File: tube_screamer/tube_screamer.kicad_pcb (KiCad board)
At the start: 2 copper layers, 80 x 100 mm, 68 parts, among them J1 Jack_6.35, J2 Jack_6.35, J3 Conn_01x05, J4 Conn_01x05, J5 Conn_01x05, J6 Barrel_Jack_Switch, J7 Conn_01x01_Socket, J8 Conn_01x01_Socket, P1 tube_screamer_front_panel, Q1 MMBT5551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

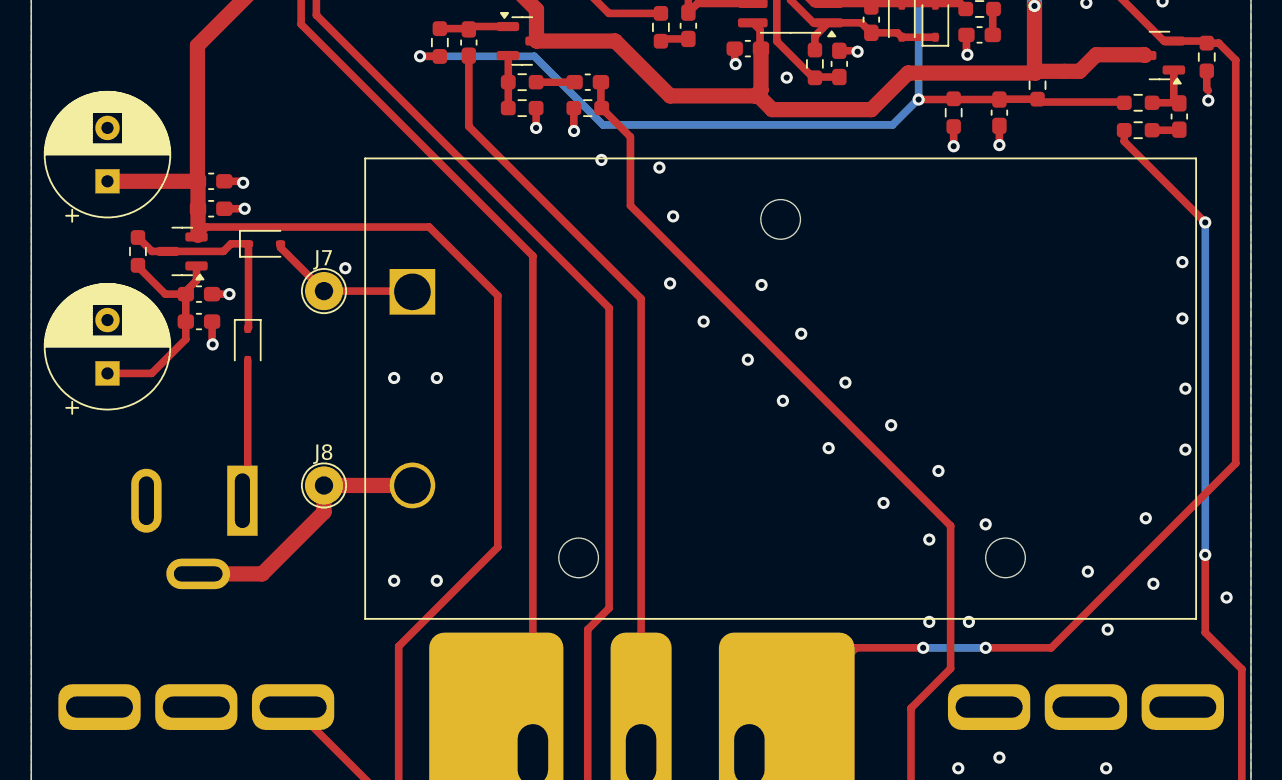
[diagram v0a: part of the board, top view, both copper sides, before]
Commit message: Pots fit, battery holder has to be moved.
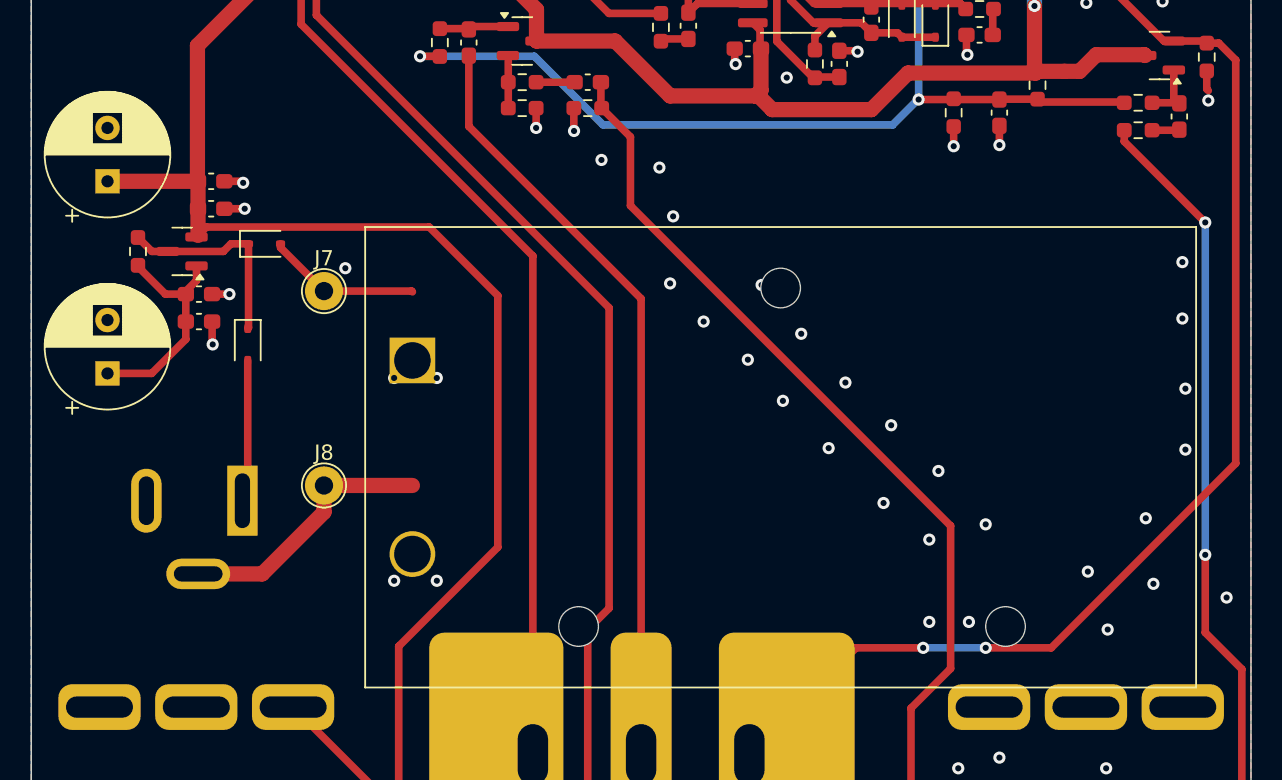
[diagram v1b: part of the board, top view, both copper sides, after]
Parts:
- moved BT1 4.50 mm to (75.0, 94.2)

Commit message: Update library.
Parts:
- moved BT1 0.05 mm to (75.0, 94.1)
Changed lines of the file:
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@@
 		(locked yes)
 		(layer "F.Cu")
-		(at 75 94.15 180)
+		(at 75 94.1 180)
 		(descr "https://eu.mouser.com/datasheet/2/209/EPD-200766-1274481.pdf")
 		(tags "9V Battery Holder")

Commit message: Updated, added 3d bodies.
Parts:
- added P2: bottom_plate, pedale:bottom_plate, F.Cu at (50.0, 50.0)
- P1: value tube_screamer_front_panel -> front_plate; footprint pedale:tube_screamer_front_plate -> pedale:front_plate
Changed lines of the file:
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@@
 		)
 		(embedded_fonts no)
-		(model "${KICAD9_3DMODEL_DIR}/Battery.3dshapes/BatteryHolder_Eagle_12BH611-GR.wrl"
+		(model "${KIPRJMOD}/../pedale.pretty/9V-battery_holder.step"
 			(offset
-				(xyz 0 0 0)
+				(xyz -25 6.5 0)
 			)
 			(scale
@@
 			)
 			(rotate
-				(xyz 0 0 0)
+				(xyz -0 -0 -0)
 			)
 		)
@@
 		(model "${KIPRJMOD}/../pedale.pretty/M3x8 Philips Screw.stp"
 			(offset
-				(xyz 0 0 -1.5)
+				(xyz 0 0 -8)
 			)
 			(scale
@@
 			)
 		)
+		(model "${KIPRJMOD}/../pedale.pretty/Abstandhalter M3 IG-AG 5mm+6mm - PA 66.stp"
+			(offset
+				(xyz 0 0 -4)
+			)
+			(scale
+				(xyz 1 1 1)
+			)
+			(rotate
+				(xyz -0 90 -0)
+			)
+		)
 	)
 	(footprint "pedale:M3_hole_with_spacer"
@@
 		(model "${KIPRJMOD}/../pedale.pretty/M3x8 Philips Screw.stp"
 			(offset
-				(xyz 0 0 -1.5)
+				(xyz 0 0 -8)
 			)
 			(scale
@@
 			)
 		)
+		(model "${KIPRJMOD}/../pedale.pretty/Abstandhalter M3 IG-AG 5mm+6mm - PA 66.stp"
+			(offset
+				(xyz 0 0 -4)
+			)
+			(scale
+				(xyz 1 1 1)
+			)
+			(rotate
+				(xyz -0 90 -0)
+			)
+		)
 	)
 	(footprint "Capacitor_SMD:C_0603_1608Metric_Pad1.08x0.95mm_HandSolder"
@@
 		)
 	)
+	(footprint "pedale:bottom_plate"
+		(layer "F.Cu")
+		(at 50 50)
+		(property "Reference" "P2"
+			(at 0 -0.5 0)
+			(unlocked yes)
+			(layer "F.SilkS")
+			(hide yes)
+			(effects
+				(font
+					(size 1 1)
+					(thickness 0.1)
+				)
+			)
+		)
+		(property "Value" "bottom_plate"
+			(at 0 1 0)
+			(unlocked yes)
+			(layer "F.Fab")
+			(effects
+				(font
+					(size 1 1)
+					(thickness 0.15)
+				)
+			)
+		)
+		(property "Datasheet" ""
+			(at 0 0 0)
+			(unlocked yes)
+			(layer "F.Fab")
+			(hide yes)
+			(effects
+				(font
+					(size 1 1)
+					(thickness 0.15)
+				)
+			)
+		)
+		(property "Description" "Potentiometer"
+			(at 0 0 0)
+			(unlocked yes)
+			(layer "F.Fab")
+			(hide yes)
+			(effects
+				(font
+					(size 1 1)
+					(thickness 0.15)
+				)
+			)
+		)
+		(property ki_fp_filters "Potentiometer*")
+		(sheetname "/")
+		(sheetfile "tube_screamer.kicad_sch")
+		(attr through_hole)
+		(fp_rect
+			(start -0.1 -0.1)
+			(end 0.1 0.1)
+			(stroke
+				(width 0.05)
+				(type default)
+			)
+			(fill no)
+			(layer "B.CrtYd")
+		)
+		(fp_text user "${REFERENCE}"
+			(at 0 2.5 0)
+			(unlocked yes)
+			(layer "F.Fab")
+			(effects
+				(font
+					(size 1 1)
+					(thickness 0.15)
+				)
+			)
+		)
+		(embedded_fonts no)
+		(model "${KIPRJMOD}/../bottom_plate.step"
+			(offset
+				(xyz 0 0 -8)
+			)
+			(scale
+				(xyz 1 1 1)
+			)
+			(rotate
+				(xyz -0 -0 -0)
+			)
+		)
+	)
 	(footprint "Resistor_SMD:R_0603_1608Metric_Pad0.98x0.95mm_HandSolder"
 		(layer "F.Cu")
@@
 		(model "${KIPRJMOD}/../pedale.pretty/M3x8 Philips Screw.stp"
 			(offset
-				(xyz 0 0 -1.5)
+				(xyz 0 0 -8)
 			)
 			(scale
@@
 			)
 		)
+		(model "${KIPRJMOD}/../pedale.pretty/Abstandhalter M3 IG-AG 5mm+6mm - PA 66.stp"
+			(offset
+				(xyz 0 0 -4)
+			)
+			(scale
+				(xyz 1 1 1)
+			)
+			(rotate
+				(xyz -0 90 -0)
+			)
+		)
 	)
 	(footprint "Capacitor_SMD:C_0603_1608Metric_Pad1.08x0.95mm_HandSolder"
@@
 		(model "${KIPRJMOD}/../pedale.pretty/M3x8 Philips Screw.stp"
 			(offset
-				(xyz 0 0 -1.5)
+				(xyz 0 0 -8)
 			)
 			(scale
@@
 			)
 		)
+		(model "${KIPRJMOD}/../pedale.pretty/Abstandhalter M3 IG-AG 5mm+6mm - PA 66.stp"
+			(offset
+				(xyz 0 0 -4)
+			)
+			(scale
+				(xyz 1 1 1)
+			)
+			(rotate
+				(xyz -0 90 -0)
+			)
+		)
 	)
 	(footprint "Resistor_SMD:R_0603_1608Metric_Pad0.98x0.95mm_HandSolder"
@@
 		)
 	)
-	(footprint "pedale:tube_screamer_front_plate"
+	(footprint "pedale:front_plate"
 		(layer "F.Cu")
 		(at 50 50)
@@
 			)
 		)
-		(property "Value" "tube_screamer_front_panel"
+		(property "Value" "front_plate"
 			(at 0 1 0)
 			(unlocked yes)
@@
 		)
 		(embedded_fonts no)
-		(model "/home/ostoja/Elektronika/pedale/tube_screamer/top_plate.step"
+		(model "${KIPRJMOD}/../top_plate.step"
 			(offset
 				(xyz 0 0 25)
@@
 		(model "${KIPRJMOD}/../pedale.pretty/M3x8 Philips Screw.stp"
 			(offset
-				(xyz 0 0 -1.5)
+				(xyz 0 0 -8)
 			)
 			(scale
@@
 			)
 		)
+		(model "${KIPRJMOD}/../pedale.pretty/Abstandhalter M3 IG-AG 5mm+6mm - PA 66.stp"
+			(offset
+				(xyz 0 0 -4)
+			)
+			(scale
+				(xyz 1 1 1)
+			)
+			(rotate
+				(xyz -0 90 -0)
+			)
+		)

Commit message: Update schematic.
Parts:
- removed D3, D5: 1N4148WS, Diode_SMD:D_SOD-323
- removed D8: floating_green_led, pedale:floating_green_led
- removed D9: floating_red_led, pedale:floating_red_led
- removed J3, J4, J5: Conn_01x05, Connector_JST:JST_EH_B5B-EH-A_1x05_P2.50mm_Vertical
- removed R18, R8: 1k, Resistor_SMD:R_0603_1608Metric_Pad0.98x0.95mm_HandSolder
- removed RV5, RV6, RV8: floating_pot, pedale:floating_pot
- added J9: top_panel_connector, Connector_IDC:IDC-Header_2x08_P2.54mm_Vertical, F.Cu at (76.9, 43.5)
- added Q10: AO3401A, Package_TO_SOT_SMD:SOT-23, F.Cu at (36.8, 83.6)
- added Q12: AO3400A, Package_TO_SOT_SMD:SOT-23, F.Cu at (36.8, 88.2)
- added Q13: AO3400A, Package_TO_SOT_SMD:SOT-23, F.Cu at (36.8, 92.9)
- added Q14: AO3400A, Package_TO_SOT_SMD:SOT-23, F.Cu at (36.8, 97.5)
- added Q6: AO3401A, Package_TO_SOT_SMD:SOT-23, F.Cu at (36.8, 74.4)
- added Q8: AO3401A, Package_TO_SOT_SMD:SOT-23, F.Cu at (36.8, 79.0)
- added R24: 100k, Resistor_SMD:R_0603_1608Metric_Pad0.98x0.95mm_HandSolder, F.Cu at (41.4, 73.2)
- added R26: 1k, Resistor_SMD:R_0603_1608Metric_Pad0.98x0.95mm_HandSolder, F.Cu at (78.8, 8.49)
- added R27: 100k, Resistor_SMD:R_0603_1608Metric_Pad0.98x0.95mm_HandSolder, F.Cu at (41.4, 75.7)
- added R28: 1k, Resistor_SMD:R_0603_1608Metric_Pad0.98x0.95mm_HandSolder, F.Cu at (78.8, 11.0)
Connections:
- net Net-(BT1-+) renamed BAT+
- net Net-(BT1--) renamed BAT-
- net Net-(D3-K) renamed REG_IN
- J1 pad R: 0 -> unconnected-(J1-PadR)
- J2 pad R: 0 -> unconnected-(J2-PadR)
- J6 pad 1: Net-(D3-A) -> CONN+
- J6 pad 2: 0 -> CONN-
- SW1 pad 4: unconnected-(SW1B-A-Pad4) -> 9V
- SW1 pad 6: 9V -> unconnected-(SW1B-C-Pad6)
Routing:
- net Net-(D3-A): track 9.34 -> 0.00 mm
- net CONN+: track 0.00 -> 9.34 mm
- net (no net): track 0.00 -> 9.12 mm
- net Net-(J5-Pin_5): track 4.83 -> 0.00 mm
- net Net-(J3-Pin_5): track 4.29 -> 0.00 mm

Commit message: 1 Red, 3 green connector.
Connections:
- J9 pad 1: 9V -> Net-(J9D-Pin_8)
- J9 pad 10: Net-(J9E-Pin_10) -> 0
- J9 pad 3: 0 -> Net-(J9E-1)
- J9 pad 8: Net-(J9D-Pin_8) -> 9V
- R26 pad 1: Net-(J9E-Pin_10) -> Net-(J9E-1)
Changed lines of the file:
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@@
 	(net 39 "Net-(J9D-Pin_8)")
 	(net 40 "unconnected-(J9G-Pin_11-Pad11)")
-	(net 41 "Net-(J9E-Pin_10)")
+	(net 41 "Net-(J9E-1)")
 	(net 42 "unconnected-(J9G-Pin_15-Pad15)")
 	(net 43 "unconnected-(J9G-Pin_13-Pad13)")
@@
 			(layers "F.Cu" "F.Mask" "F.Paste")
 			(roundrect_rratio 0.25)
-			(net 41 "Net-(J9E-Pin_10)")
+			(net 41 "Net-(J9E-1)")
 			(pintype "passive")
 		)
@@
 			(remove_unused_layers no)
 			(roundrect_rratio 0.147059)
-			(net 12 "9V")
-			(pinfunction "VCC")
+			(net 39 "Net-(J9D-Pin_8)")
+			(pinfunction "Pin_8")
 			(pintype "passive")
 		)
@@
 			(layers "*.Cu" "*.Mask")
 			(remove_unused_layers no)
-			(net 1 "0")
-			(pinfunction "GND")
+			(net 41 "Net-(J9E-1)")
+			(pinfunction "1")
 			(pintype "passive")
 		)
@@
 			(layers "*.Cu" "*.Mask")
 			(remove_unused_layers no)
-			(net 39 "Net-(J9D-Pin_8)")
-			(pinfunction "Pin_8")
+			(net 12 "9V")
+			(pinfunction "VCC")
 			(pintype "passive")
 		)
@@
 			(layers "*.Cu" "*.Mask")
 			(remove_unused_layers no)
-			(net 41 "Net-(J9E-Pin_10)")
-			(pinfunction "Pin_10")
+			(net 1 "0")
+			(pinfunction "GND")
 			(pintype "passive")
 		)

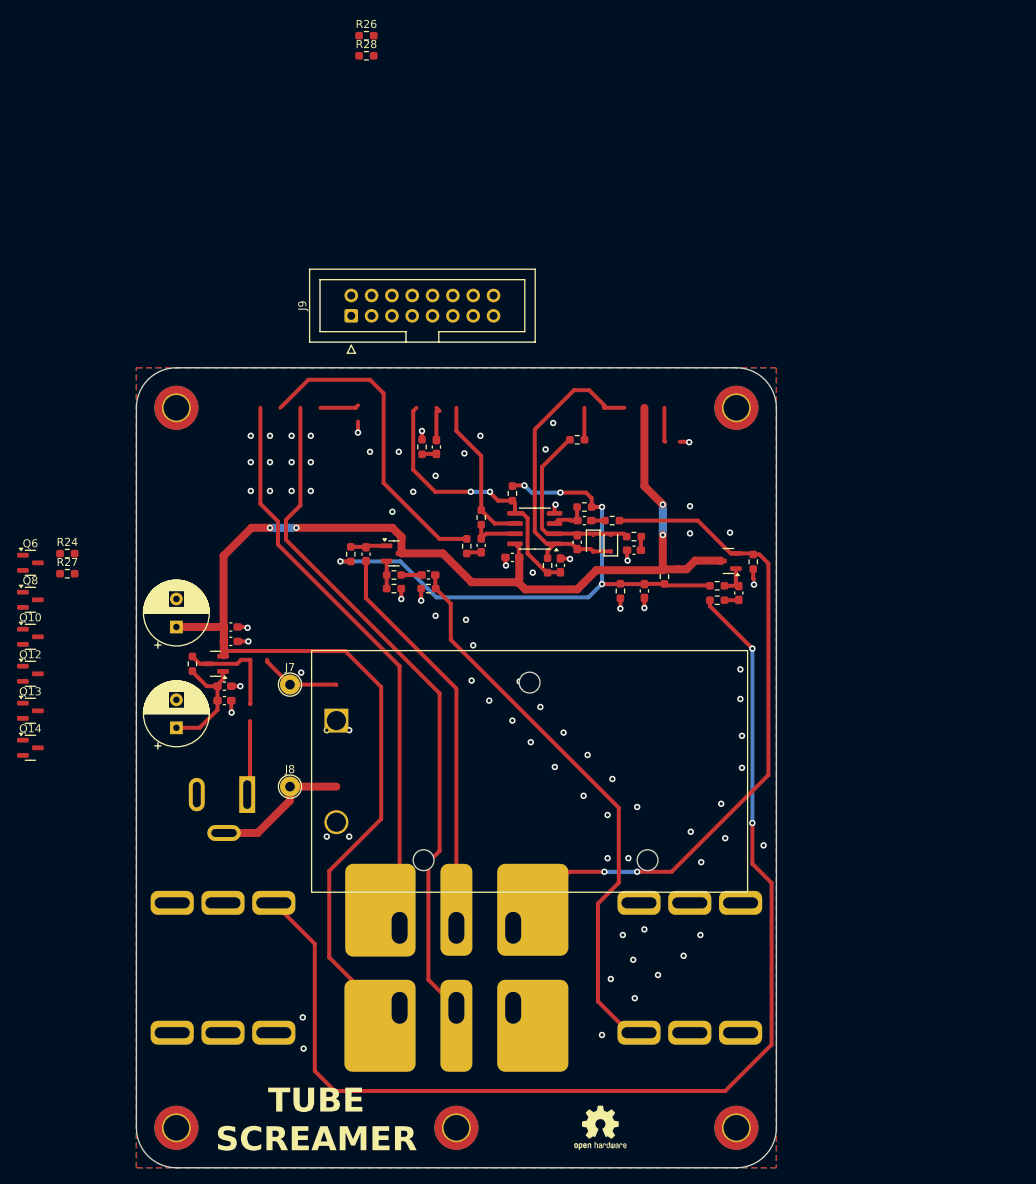
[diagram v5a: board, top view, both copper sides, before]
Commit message: Fixed diodes on front plate, fixed power schem.
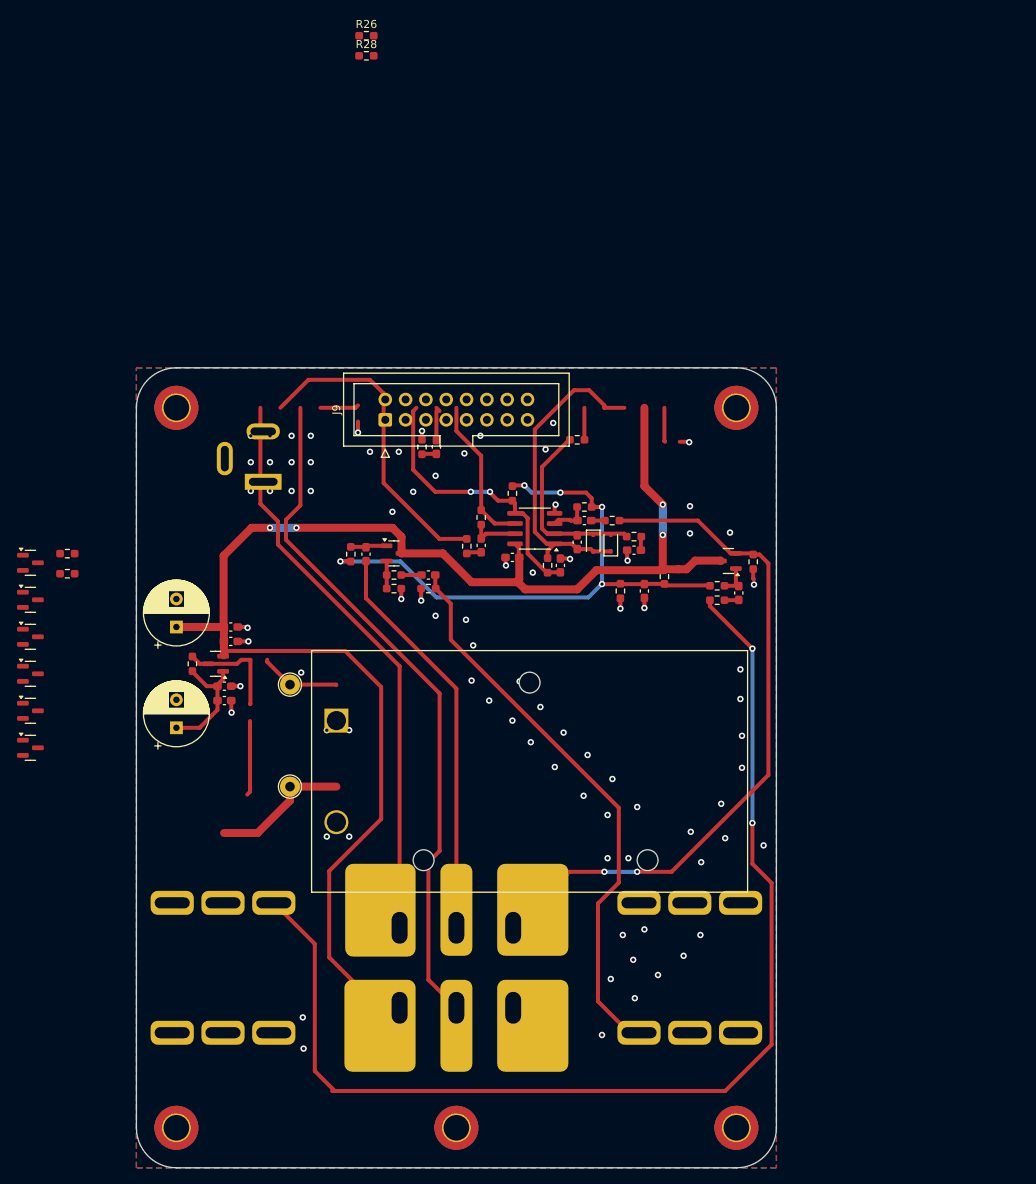
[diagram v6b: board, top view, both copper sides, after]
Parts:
- removed SIM1: Logo_Open_Hardware_Small, Symbol:OSHW-Logo2_7.3x6mm_SilkScreen
- moved J1 48.4 mm to (112.8, 116.9), turned to 0 degrees
- moved J2 48.4 mm to (67.2, 133.1), turned to 180 degrees
- moved J6 39.2 mm to (65.8, 64.2), turned to 180 degrees
- moved J9 13.7 mm to (81.1, 56.5)
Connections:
- net Net-(C11-Pad2) renamed /OUTPUT
- net Net-(D1-A) renamed /OVD
- net Net-(J1-PadT) renamed /INPUT
- net Net-(J9B-Pin_5) renamed /TON_HIGH
- net Net-(J9B-Pin_9) renamed /TON_LOW
- net Net-(SW1B-B) renamed /RED_LED
- J1 pad SN: unconnected-(J1-PadSN) -> IN_CONNECT
- Q6 pad 2: REG_IN -> BAT+
- Q6 pad 3: BAT+ -> REG_IN
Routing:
- net unconnected-(J1-PadTN): track 0.00 -> 142.8 mm, vias 0 -> 2
- net /INPUT: track 142.8 -> 0.00 mm, vias 2 -> 0
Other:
- board text removed: "TUBE SCREAMER"
